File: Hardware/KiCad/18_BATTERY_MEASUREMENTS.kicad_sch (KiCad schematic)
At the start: 0 parts

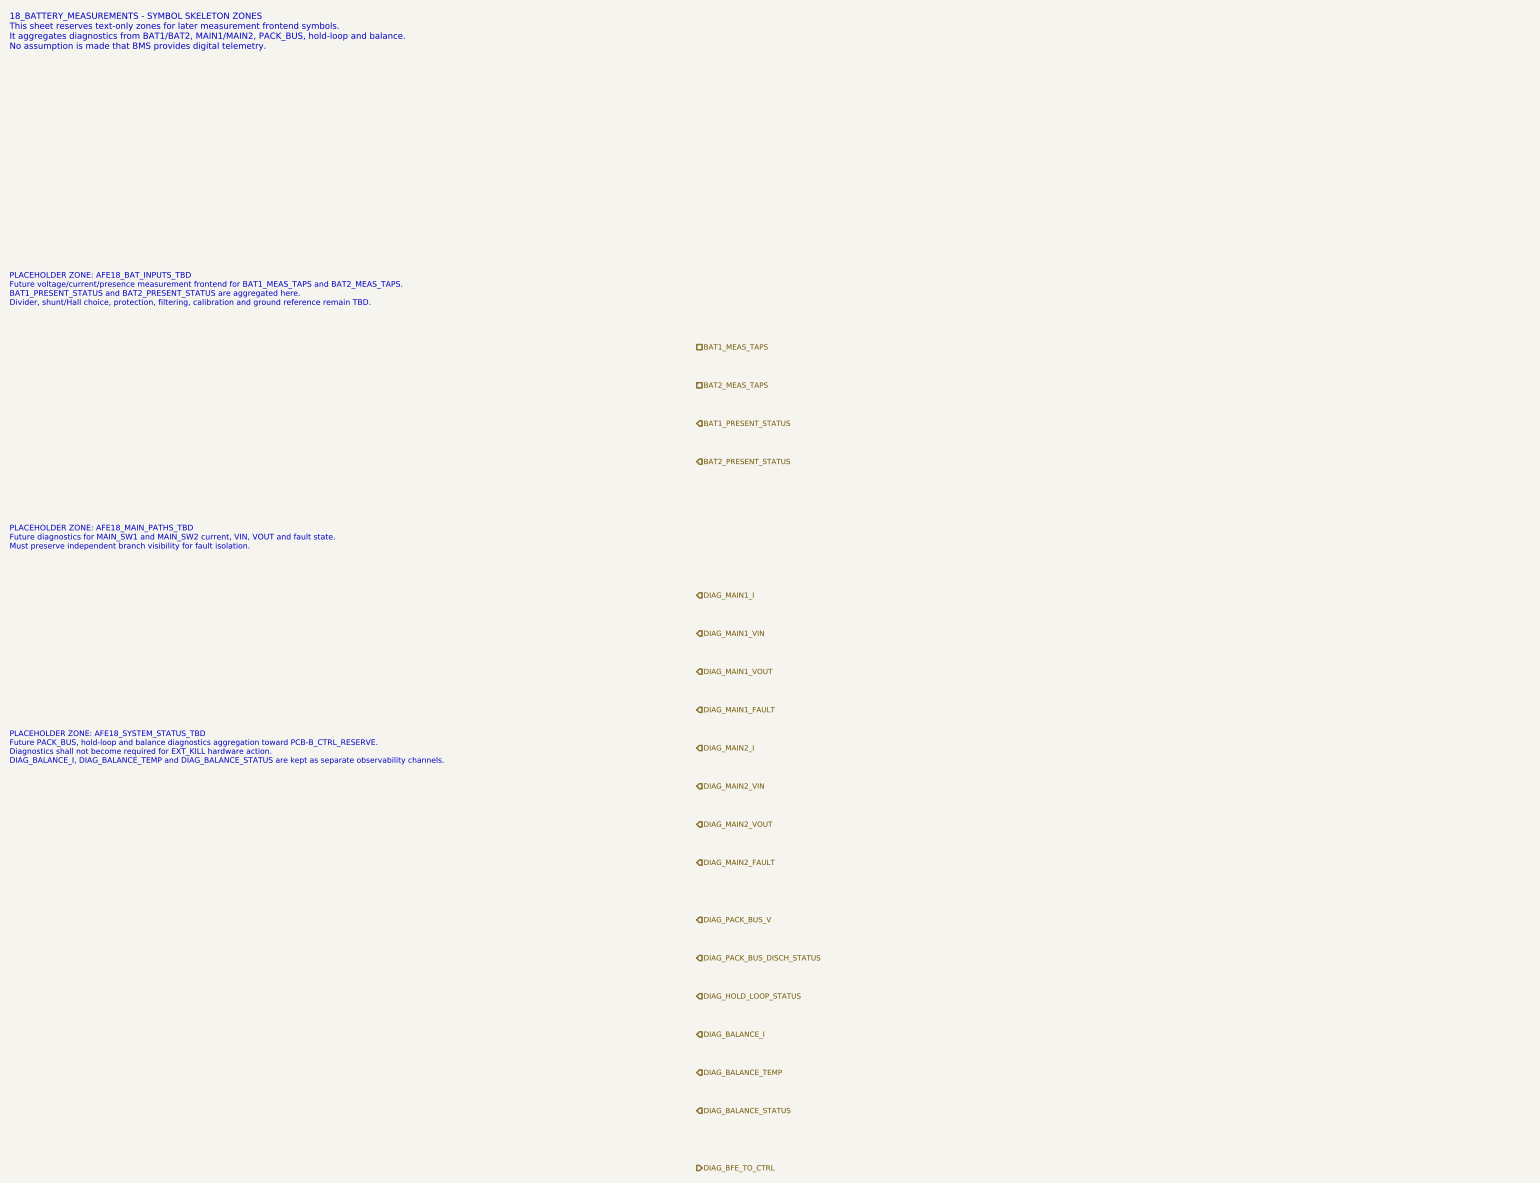
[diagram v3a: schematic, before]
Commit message: hardware: expose canonical PCB-A diagnostic interfaces
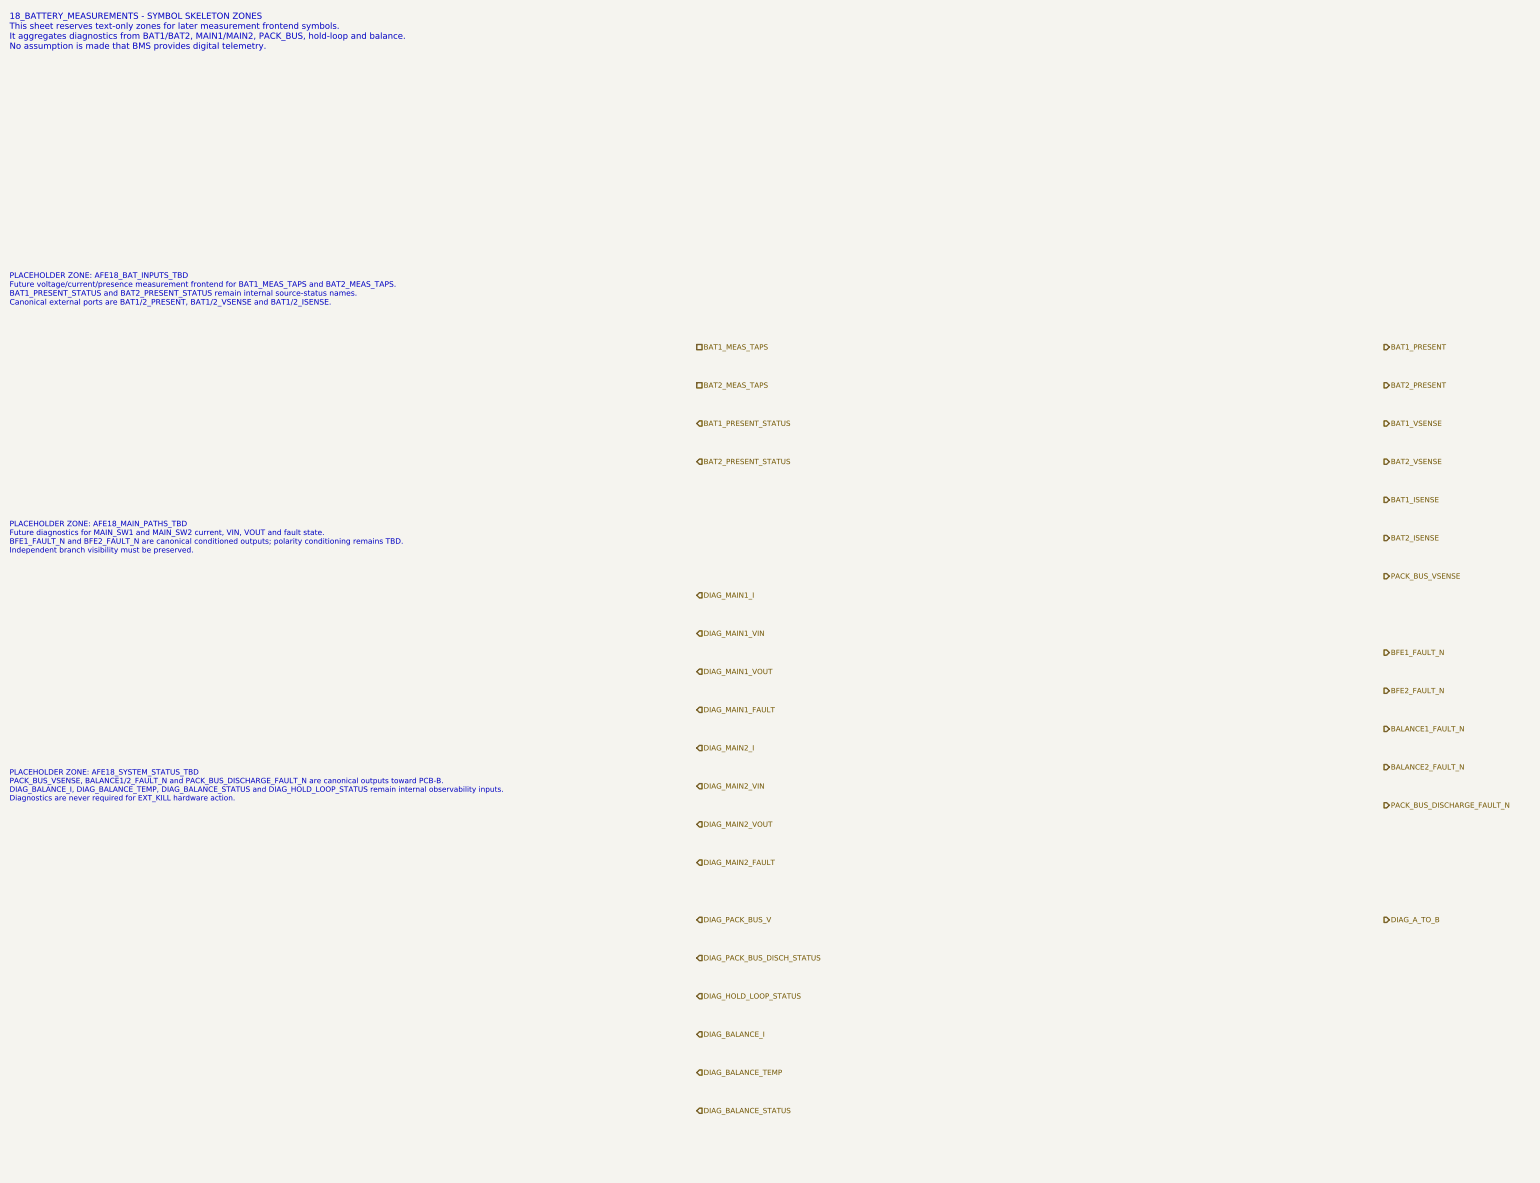
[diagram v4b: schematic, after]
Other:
- note added: "PLACEHOLDER ZONE: AFE18_BAT_INPUTS_TBD Future voltage/current/presence measurement frontend for BAT1_MEAS_TAPS and BAT2_MEAS_TAPS. BAT1_PRESENT_STATUS and BAT2_PRESENT_STATUS remain internal source-status names. Canonical external ports are BAT1/2_PRESENT, BAT1/2_VSENSE and BAT1/2_ISENSE."
- note added: "PLACEHOLDER ZONE: AFE18_MAIN_PATHS_TBD Future diagnostics for MAIN_SW1 and MAIN_SW2 current, VIN, VOUT and fault state. BFE1_FAULT_N and BFE2_FAULT_N are canonical conditioned outputs; polarity conditioning remains TBD. Independent branch visibility must be preserved."
- note added: "PLACEHOLDER ZONE: AFE18_SYSTEM_STATUS_TBD PACK_BUS_VSENSE, BALANCE1/2_FAULT_N and PACK_BUS_DISCHARGE_FAULT_N are canonical outputs toward PCB-B. DIAG_BALANCE_I, DIAG_BALANCE_TEMP, DIAG_BALANCE_STATUS and DIAG_HOLD_LOOP_STATUS remain internal observability inputs. Diagnostics are never required for EXT_KILL hardware action."
- note removed: "PLACEHOLDER ZONE: AFE18_BAT_INPUTS_TBD Future voltage/current/presence measurement frontend for BAT1_MEAS_TAPS and BAT2_MEAS_TAPS. BAT1_PRESENT_STATUS and BAT2_PRESENT_STATUS are aggregated here. Divider, shunt/Hall choice, protection, filtering, calibration and ground reference remain TBD."
- note removed: "PLACEHOLDER ZONE: AFE18_MAIN_PATHS_TBD Future diagnostics for MAIN_SW1 and MAIN_SW2 current, VIN, VOUT and fault state. Must preserve independent branch visibility for fault isolation."
- note removed: "PLACEHOLDER ZONE: AFE18_SYSTEM_STATUS_TBD Future PACK_BUS, hold-loop and balance diagnostics aggregation toward PCB-B_CTRL_RESERVE. Diagnostics shall not become required for EXT_KILL hardware action. DIAG_BALANCE_I, DIAG_BALANCE_TEMP and DIAG_BALANCE_STATUS are kept as separate observability channels."
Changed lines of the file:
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@@
 		(title "18_BATTERY_MEASUREMENTS - BFE sensing boundary")
 		(date "2026-07-15")
-		(rev "C2")
+		(rev "C3")
 		(company "Gonoboben/plataVM")
-		(comment 1 "Interface consistency: complete BFE measurement aggregation")
+		(comment 1 "Interface consistency: canonical PCB-A to PCB-B measurement and fault ports")
 		(comment 2 "No ADC frontend, isolation, sensor technology or part number selected")
 	)
@@
 		(uuid "bfe-lb-00000018-0000-4000-8000-000000000101")
 	)
-	(text "PLACEHOLDER ZONE: AFE18_BAT_INPUTS_TBD\nFuture voltage/current/presence measurement frontend for BAT1_MEAS_TAPS and BAT2_MEAS_TAPS.\nBAT1_PRESENT_STATUS and BAT2_PRESENT_STATUS are aggregated here.\nDivider, shunt/Hall choice, protection, filtering, calibration and ground reference remain TBD."
+	(text "PLACEHOLDER ZONE: AFE18_BAT_INPUTS_TBD\nFuture voltage/current/presence measurement frontend for BAT1_MEAS_TAPS and BAT2_MEAS_TAPS.\nBAT1_PRESENT_STATUS and BAT2_PRESENT_STATUS remain internal source-status names.\nCanonical external ports are BAT1/2_PRESENT, BAT1/2_VSENSE and BAT1/2_ISENSE."
 		(exclude_from_sim no)
 		(at 12 70 0)
-		(effects (font (size 1.18 1.18)) (justify left))
+		(effects (font (size 1.16 1.16)) (justify left))
 		(uuid "bfe-lb-00000018-0000-4000-8000-000000000102")
 	)
-	(text "PLACEHOLDER ZONE: AFE18_MAIN_PATHS_TBD\nFuture diagnostics for MAIN_SW1 and MAIN_SW2 current, VIN, VOUT and fault state.\nMust preserve independent branch visibility for fault isolation."
+	(text "PLACEHOLDER ZONE: AFE18_MAIN_PATHS_TBD\nFuture diagnostics for MAIN_SW1 and MAIN_SW2 current, VIN, VOUT and fault state.\nBFE1_FAULT_N and BFE2_FAULT_N are canonical conditioned outputs; polarity conditioning remains TBD.\nIndependent branch visibility must be preserved."
 		(exclude_from_sim no)
 		(at 12 122 0)
-		(effects (font (size 1.18 1.18)) (justify left))
+		(effects (font (size 1.14 1.14)) (justify left))
 		(uuid "bfe-lb-00000018-0000-4000-8000-000000000103")
 	)
-	(text "PLACEHOLDER ZONE: AFE18_SYSTEM_STATUS_TBD\nFuture PACK_BUS, hold-loop and balance diagnostics aggregation toward PCB-B_CTRL_RESERVE.\nDiagnostics shall not become required for EXT_KILL hardware action.\nDIAG_BALANCE_I, DIAG_BALANCE_TEMP and DIAG_BALANCE_STATUS are kept as separate observability channels."
+	(text "PLACEHOLDER ZONE: AFE18_SYSTEM_STATUS_TBD\nPACK_BUS_VSENSE, BALANCE1/2_FAULT_N and PACK_BUS_DISCHARGE_FAULT_N are canonical outputs toward PCB-B.\nDIAG_BALANCE_I, DIAG_BALANCE_TEMP, DIAG_BALANCE_STATUS and DIAG_HOLD_LOOP_STATUS remain internal observability inputs.\nDiagnostics are never required for EXT_KILL hardware action."
 		(exclude_from_sim no)
-		(at 12 166 0)
-		(effects (font (size 1.16 1.16)) (justify left))
+		(at 12 174 0)
+		(effects (font (size 1.12 1.12)) (justify left))
 		(uuid "bfe-lb-00000018-0000-4000-8000-000000000104")
 	)
@@
 	(hierarchical_label "DIAG_BALANCE_TEMP" (shape input) (exclude_from_sim no) (at 156 234 0) (effects (font (size 1.1 1.1)) (justify left)) (uuid "bfe-lb-00000018-0000-4000-8000-000000000219"))
 	(hierarchical_label "DIAG_BALANCE_STATUS" (shape input) (exclude_from_sim no) (at 156 242 0) (effects (font (size 1.1 1.1)) (justify left)) (uuid "bfe-lb-00000018-0000-4000-8000-000000000214"))
-	(hierarchical_label "DIAG_BFE_TO_CTRL" (shape output) (exclude_from_sim no) (at 156 254 0) (effects (font (size 1.1 1.1)) (justify left)) (uuid "bfe-lb-00000018-0000-4000-8000-000000000215"))
+	(hierarchical_label "BAT1_PRESENT" (shape output) (exclude_from_sim no) (at 300 82 0) (effects (font (size 1.1 1.1)) (justify left)) (uuid "bfe-lb-00000018-0000-4000-8000-000000000220"))
+	(hierarchical_label "BAT2_PRESENT" (shape output) (exclude_from_sim no) (at 300 90 0) (effects (font (size 1.1 1.1)) (justify left)) (uuid "bfe-lb-00000018-0000-4000-8000-000000000221"))
+	(hierarchical_label "BAT1_VSENSE" (shape output) (exclude_from_sim no) (at 300 98 0) (effects (font (size 1.1 1.1)) (justify left)) (uuid "bfe-lb-00000018-0000-4000-8000-000000000222"))
+	(hierarchical_label "BAT2_VSENSE" (shape output) (exclude_from_sim no) (at 300 106 0) (effects (font (size 1.1 1.1)) (justify left)) (uuid "bfe-lb-00000018-0000-4000-8000-000000000223"))
+	(hierarchical_label "BAT1_ISENSE" (shape output) (exclude_from_sim no) (at 300 114 0) (effects (font (size 1.1 1.1)) (justify left)) (uuid "bfe-lb-00000018-0000-4000-8000-000000000224"))
+	(hierarchical_label "BAT2_ISENSE" (shape output) (exclude_from_sim no) (at 300 122 0) (effects (font (size 1.1 1.1)) (justify left)) (uuid "bfe-lb-00000018-0000-4000-8000-000000000225"))
+	(hierarchical_label "PACK_BUS_VSENSE" (shape output) (exclude_from_sim no) (at 300 130 0) (effects (font (size 1.1 1.1)) (justify left)) (uuid "bfe-lb-00000018-0000-4000-8000-000000000226"))
+	(hierarchical_label "BFE1_FAULT_N" (shape output) (exclude_from_sim no) (at 300 146 0) (effects (font (size 1.1 1.1)) (justify left)) (uuid "bfe-lb-00000018-0000-4000-8000-000000000227"))
+	(hierarchical_label "BFE2_FAULT_N" (shape output) (exclude_from_sim no) (at 300 154 0) (effects (font (size 1.1 1.1)) (justify left)) (uuid "bfe-lb-00000018-0000-4000-8000-000000000228"))
+	(hierarchical_label "BALANCE1_FAULT_N" (shape output) (exclude_from_sim no) (at 300 162 0) (effects (font (size 1.1 1.1)) (justify left)) (uuid "bfe-lb-00000018-0000-4000-8000-000000000229"))
+	(hierarchical_label "BALANCE2_FAULT_N" (shape output) (exclude_from_sim no) (at 300 170 0) (effects (font (size 1.1 1.1)) (justify left)) (uuid "bfe-lb-00000018-0000-4000-8000-000000000230"))
+	(hierarchical_label "PACK_BUS_DISCHARGE_FAULT_N" (shape output) (exclude_from_sim no) (at 300 178 0) (effects (font (size 1.1 1.1)) (justify left)) (uuid "bfe-lb-00000018-0000-4000-8000-000000000231"))
+	(hierarchical_label "DIAG_A_TO_B" (shape output) (exclude_from_sim no) (at 300 202 0) (effects (font (size 1.1 1.1)) (justify left)) (uuid "bfe-lb-00000018-0000-4000-8000-000000000215"))
 )
